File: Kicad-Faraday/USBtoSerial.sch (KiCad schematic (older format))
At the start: 10 parts, among them P16 USB-MICRO-B, U10 NUF2101MT1G, U6 FT230XQ-R

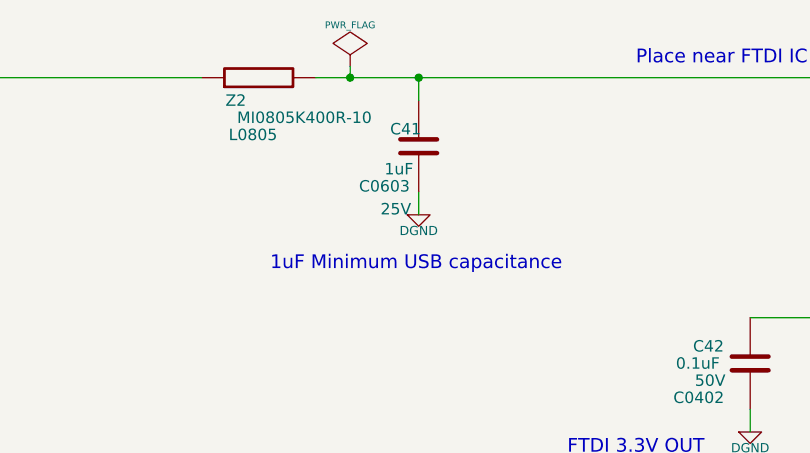
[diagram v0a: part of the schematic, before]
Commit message: Removed basic parts I don't really need to test or am so confident that testing will be fine I'm OK making the changes well in advance
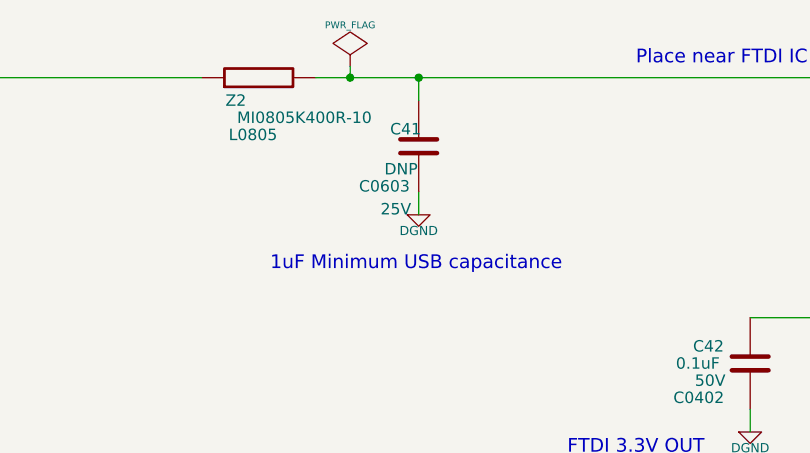
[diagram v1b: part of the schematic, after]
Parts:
- C41: value 1uF -> DNP
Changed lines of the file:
@@
 Sheet 8 11
 Title "Faraday Wireless Node"
-Date "24 oct 2016"
+Date "2 nov 2016"
 Rev "C"
 Comp "FaradayRF"
@@
 $EndComp
 $Comp
-L PWR_FLAG #FLG078
+L PWR_FLAG #FLG077
 U 1 1 54090954
 P 800 6000
-F 0 "#FLG078" H 800 6095 30  0001 C CNN
+F 0 "#FLG077" H 800 6095 30  0001 C CNN
 F 1 "PWR_FLAG" H 800 6180 30  0000 C CNN
 F 2 "" H 800 6000 60  0000 C CNN
@@
 5V USB
 $Comp
-L PWR_FLAG #FLG079
+L PWR_FLAG #FLG078
 U 1 1 54170CB7
 P 7000 4550
-F 0 "#FLG079" H 7000 4645 30  0001 C CNN
+F 0 "#FLG078" H 7000 4645 30  0001 C CNN
 F 1 "PWR_FLAG" H 7000 4730 30  0000 C CNN
 F 2 "" H 7000 4550 60  0000 C CNN
@@
 FTDI 3.3V OUT\nPower Flag
 $Comp
-L PWR_FLAG #FLG080
+L PWR_FLAG #FLG079
 U 1 1 541715EA
 P 5250 2650
-F 0 "#FLG080" H 5250 2745 30  0001 C CNN
+F 0 "#FLG079" H 5250 2745 30  0001 C CNN
 F 1 "PWR_FLAG" H 5250 2830 30  0000 C CNN
 F 2 "" H 5250 2650 60  0000 C CNN
@@
 $EndComp
 $Comp
-L DGND #PWR081
+L DGND #PWR080
 U 1 1 55A55E2C
 P 8350 6000
-F 0 "#PWR081" H 8350 6000 40  0001 C CNN
+F 0 "#PWR080" H 8350 6000 40  0001 C CNN
 F 1 "DGND" H 8350 5930 40  0000 C CNN
 F 2 "~" H 8350 6000 60  0000 C CNN
@@
 $EndComp
 $Comp
-L DGND #PWR082
+L DGND #PWR081
 U 1 1 55A55E8C
 P 7000 4250
-F 0 "#PWR082" H 7000 4250 40  0001 C CNN
+F 0 "#PWR081" H 7000 4250 40  0001 C CNN
 F 1 "DGND" H 7000 4180 40  0000 C CNN
 F 2 "~" H 7000 4250 60  0000 C CNN
@@
 $EndComp
 $Comp
-L DGND #PWR083
+L DGND #PWR082
 U 1 1 55A55E92
 P 7600 3300
-F 0 "#PWR083" H 7600 3300 40  0001 C CNN
+F 0 "#PWR082" H 7600 3300 40  0001 C CNN
 F 1 "DGND" H 7600 3230 40  0000 C CNN
 F 2 "~" H 7600 3300 60  0000 C CNN
@@
 $EndComp
 $Comp
-L DGND #PWR084
+L DGND #PWR083
 U 1 1 55A55E9E
 P 2100 6900
-F 0 "#PWR084" H 2100 6900 40  0001 C CNN
+F 0 "#PWR083" H 2100 6900 40  0001 C CNN
 F 1 "DGND" H 2100 6830 40  0000 C CNN
 F 2 "~" H 2100 6900 60  0000 C CNN
@@
 $EndComp
 $Comp
-L DGND #PWR085
+L DGND #PWR084
 U 1 1 55A55EA4
 P 1550 6900
-F 0 "#PWR085" H 1550 6900 40  0001 C CNN
+F 0 "#PWR084" H 1550 6900 40  0001 C CNN
 F 1 "DGND" H 1550 6830 40  0000 C CNN
 F 2 "~" H 1550 6900 60  0000 C CNN
@@
 $EndComp
 $Comp
-L +5V #PWR086
+L +5V #PWR085
 U 1 1 5788A803
 P 8250 2700
-F 0 "#PWR086" H 8250 2790 20  0001 C CNN
+F 0 "#PWR085" H 8250 2790 20  0001 C CNN
 F 1 "+5V" H 8250 2790 30  0000 C CNN
 F 2 "" H 8250 2700 60  0000 C CNN
@@
 P 5550 3000
 F 0 "C41" H 5425 3075 50  0000 L CNN
-F 1 "1uF" H 5400 2900 50  0000 L CNN
+F 1 "DNP" H 5400 2900 50  0000 L CNN
 F 2 "C0603" H 5400 2825 50  0000 C CNN
 F 3 "" H 5550 3000 60  0000 C CNN
@@
 $EndComp
 $Comp
-L DGND #PWR087
+L DGND #PWR086
 U 1 1 578BD7EF
 P 5550 3300
-F 0 "#PWR087" H 5550 3300 40  0001 C CNN
+F 0 "#PWR086" H 5550 3300 40  0001 C CNN
 F 1 "DGND" H 5550 3230 40  0000 C CNN
 F 2 "~" H 5550 3300 60  0000 C CNN
@@
 $EndComp
 $Comp
-L DGND #PWR088
+L DGND #PWR087
 U 1 1 578CED94
 P 1100 6900
-F 0 "#PWR088" H 1100 6900 40  0001 C CNN
+F 0 "#PWR087" H 1100 6900 40  0001 C CNN
 F 1 "DGND" H 1100 6830 40  0000 C CNN
 F 2 "~" H 1100 6900 60  0000 C CNN
@@
 $EndComp
 $Comp
-L GNDPWR #PWR089
+L GNDPWR #PWR088
 U 1 1 578D0220
 P 800 6900
-F 0 "#PWR089" H 800 6950 40  0001 C CNN
+F 0 "#PWR088" H 800 6950 40  0001 C CNN
 F 1 "GNDPWR" H 800 6820 40  0000 C CNN
 F 2 "" H 800 6900 60  0000 C CNN
@@
 1Meg resistor for shield dischard\n4.7nF capacitor for RF noise
 $Comp
-L PWR_FLAG #FLG090
+L PWR_FLAG #FLG089
 U 1 1 578DEE25
 P 2300 6000
-F 0 "#FLG090" H 2300 6095 30  0001 C CNN
+F 0 "#FLG089" H 2300 6095 30  0001 C CNN
 F 1 "PWR_FLAG" H 2300 6180 30  0000 C CNN
 F 2 "" H 2300 6000 60  0000 C CNN
